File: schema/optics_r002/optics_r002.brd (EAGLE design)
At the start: 65 x 38 mm, 81 parts, among them U3 iC-HKB, X3 MikroBus_3, X4 PAN_SERVO, X5 TILT_SERVO

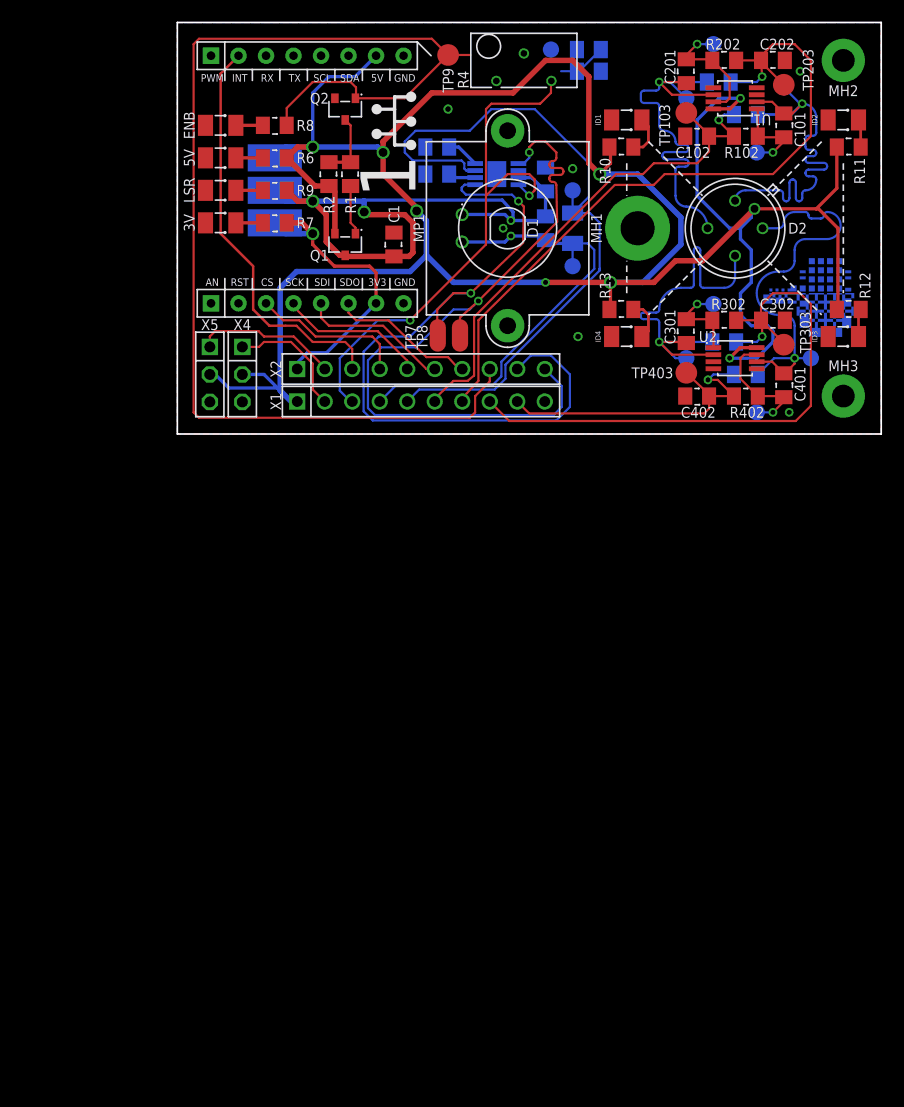
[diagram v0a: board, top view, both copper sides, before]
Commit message: updated reworks 1-4 to schematic r002
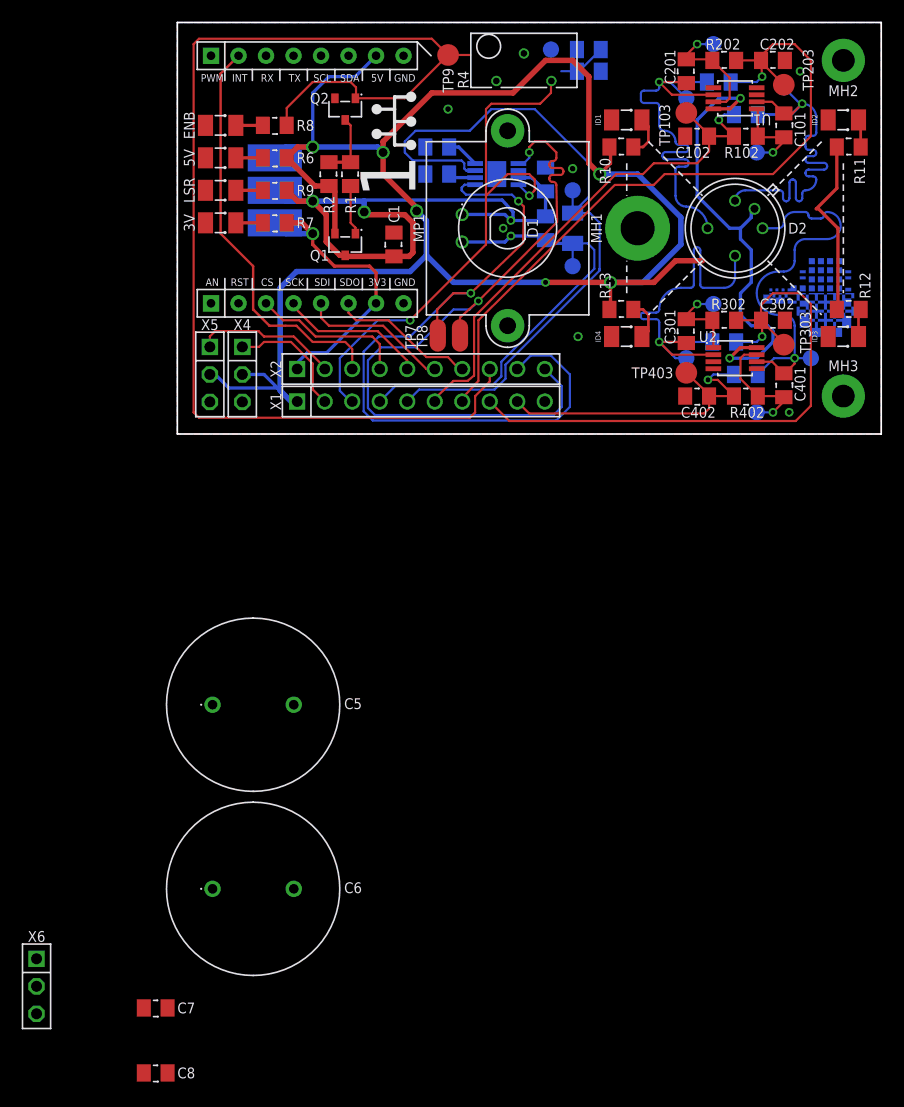
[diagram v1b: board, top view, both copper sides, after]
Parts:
- added C5, C6: 4700u, rcl:RADIAL_21_16_35
- added C7, C8: 0.1u, rcl:0805_WAVE
- added X6: REWORK, io:22-28-4030
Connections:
- new net GND_A: X6.2
- new net P12V: D2.5, X6.1
- net GND: now also C5.2, C6.2, C7.2, C8.2, X6.3
- net P5V: now also C5.1, C6.1, C7.1, C8.1; no longer D2.5
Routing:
- net P5V: track 243.3 -> 230.4 mm
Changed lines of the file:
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@@
 <attribute name="MFR" value="Cree" x="26.3" y="19" size="1.778" layer="28" rot="MR270" display="off"/>
+</element>
+<element name="C5" library="rcl" package="RADIAL_21_16_35" value="4700u" x="7" y="-25">
+<attribute name="EAGLEUP" value="RADIAL_21_16_35" x="7" y="-25" size="1.778" layer="27" display="off"/>
+<attribute name="TOL" value="20" x="7" y="-25" size="1.778" layer="27" display="off"/>
+</element>
+<element name="C6" library="rcl" package="RADIAL_21_16_35" value="4700u" x="7" y="-42">
+<attribute name="EAGLEUP" value="RADIAL_21_16_35" x="7" y="-42" size="1.778" layer="27" display="off"/>
+<attribute name="TOL" value="20" x="7" y="-42" size="1.778" layer="27" display="off"/>
+</element>
+<element name="C7" library="rcl" package="0805_WAVE" value="0.1u" x="-2" y="-53">
+<attribute name="EAGLEUP" value="C0805;;" x="-2" y="-53" size="1.778" layer="27" display="off"/>
+<attribute name="TOL" value="5" x="-2" y="-53" size="1.778" layer="27" display="off"/>
+</element>
+<element name="C8" library="rcl" package="0805_WAVE" value="0.1u" x="-2" y="-59">
+<attribute name="EAGLEUP" value="C0805;;" x="-2" y="-59" size="1.778" layer="27" display="off"/>
+<attribute name="TOL" value="5" x="-2" y="-59" size="1.778" layer="27" display="off"/>
+</element>
+<element name="X6" library="io" package="22-28-4030" value="REWORK" x="-13" y="-51">
+<attribute name="MFR" value="Molex" x="-13" y="-51" size="1.778" layer="27" display="off"/>
+<attribute name="EAGLEUP" value="HEADER_MALE_1X03;;" x="-13" y="-51" size="1.778" layer="27" display="off"/>
+<attribute name="MPN" value="22-28-4030" x="-13" y="-51" size="1.778" layer="27" display="off"/>
+<attribute name="CIRCUITS" value="3" x="-13" y="-51" size="1.778" layer="27" display="off"/>
 </element>
 </elements>
@@
 <vertex x="0" y="38"/>
 </polygon>
+<contactref element="C5" pad="2"/>
+<contactref element="C6" pad="2"/>
+<contactref element="C7" pad="2"/>
+<contactref element="C8" pad="2"/>
+<contactref element="X6" pad="3"/>
+<wire x1="57.5" y1="33.5" x2="61.5" y2="34.5" width="0" layer="19" extent="1-1"/>
+<wire x1="56.1" y1="34.5" x2="57.5" y2="33.5" width="0" layer="19" extent="1-1"/>
+<wire x1="53.5" y1="31.975" x2="56.1" y2="34.5" width="0" layer="19" extent="1-1"/>
+<wire x1="53.5" y1="31.325" x2="53.5" y2="31.975" width="0" layer="19" extent="1-1"/>
+<wire x1="49.5" y1="31.975" x2="53.5" y2="31.975" width="0" layer="19" extent="1-1"/>
+<wire x1="46.9" y1="27.5" x2="49.5" y2="31.975" width="0" layer="19" extent="1-1"/>
+<wire x1="60.1" y1="29" x2="57.5" y2="33.5" width="0" layer="19" extent="1-1"/>
+<wire x1="40.1" y1="29" x2="46.9" y2="27.5" width="0" layer="19" extent="1-1"/>
+<wire x1="39.1" y1="33.5" x2="40.1" y2="29" width="0" layer="19" extent="1-16"/>
+<wire x1="36.9" y1="35.5" x2="39.1" y2="33.5" width="0" layer="19" extent="16-16"/>
+<wire x1="36.5" y1="24.5" x2="40.1" y2="29" width="0" layer="19" extent="1-1"/>
+<wire x1="34" y1="24.6" x2="36.5" y2="24.5" width="0" layer="19" extent="16-16"/>
+<wire x1="31.5" y1="24.325" x2="34" y2="24.6" width="0" layer="19" extent="16-16"/>
+<wire x1="29.5" y1="24" x2="31.5" y2="24.325" width="0" layer="19" extent="16-16"/>
+<wire x1="30.5" y1="28" x2="31.5" y2="24.325" width="0" layer="19" extent="16-16"/>
+<wire x1="30.085" y1="19" x2="29.5" y2="24" width="0" layer="19" extent="16-16"/>
+<wire x1="25" y1="30" x2="30.5" y2="28" width="0" layer="19" extent="1-1"/>
+<wire x1="22.9" y1="26.5" x2="25" y2="30" width="0" layer="19" extent="16-16"/>
+<wire x1="22.9" y1="24" x2="22.9" y2="26.5" width="0" layer="19" extent="16-16"/>
+<wire x1="20" y1="18.6" x2="22.9" y2="24" width="0" layer="19" extent="1-16"/>
+<wire x1="20.89" y1="34.93" x2="25" y2="30" width="0" layer="19" extent="1-1"/>
+<wire x1="20.89" y1="12.07" x2="20" y2="18.6" width="0" layer="19" extent="1-1"/>
+<wire x1="14.55" y1="31" x2="20.89" y2="34.93" width="0" layer="19" extent="1-1"/>
+<wire x1="42.5" y1="19" x2="36.5" y2="24.5" width="0" layer="19" extent="1-1"/>
+<wire x1="30.5" y1="10" x2="30.085" y2="19" width="0" layer="19" extent="1-1"/>
+<wire x1="37" y1="9" x2="30.5" y2="10" width="0" layer="19" extent="1-1"/>
+<wire x1="40.1" y1="9" x2="37" y2="9" width="0" layer="19" extent="1-1"/>
+<wire x1="33.93" y1="3" x2="37" y2="9" width="0" layer="19" extent="1-1"/>
+<wire x1="46.9" y1="3.5" x2="40.1" y2="9" width="0" layer="19" extent="1-1"/>
+<wire x1="49.5" y1="6.025" x2="46.9" y2="3.5" width="0" layer="19" extent="1-1"/>
+<wire x1="49.5" y1="6.675" x2="49.5" y2="6.025" width="0" layer="19" extent="1-1"/>
+<wire x1="53.5" y1="6.025" x2="49.5" y2="6.025" width="0" layer="19" extent="1-1"/>
+<wire x1="56.5" y1="2" x2="53.5" y2="6.025" width="0" layer="19" extent="1-1"/>
+<wire x1="56.1" y1="10.5" x2="53.5" y2="6.025" width="0" layer="19" extent="1-1"/>
+<wire x1="60.1" y1="9" x2="56.1" y2="10.5" width="0" layer="19" extent="1-1"/>
+<wire x1="61.5" y1="3.5" x2="56.5" y2="2" width="0" layer="19" extent="1-1"/>
+<wire x1="2.6" y1="28.5" x2="14.55" y2="31" width="0" layer="19" extent="1-1"/>
+<wire x1="2.6" y1="25.5" x2="2.6" y2="28.5" width="0" layer="19" extent="1-1"/>
+<wire x1="2.6" y1="22.5" x2="2.6" y2="25.5" width="0" layer="19" extent="1-1"/>
+<wire x1="2.6" y1="19.5" x2="2.6" y2="22.5" width="0" layer="19" extent="1-1"/>
+<wire x1="3" y1="2.96" x2="2.6" y2="19.5" width="0" layer="19" extent="1-1"/>
+<wire x1="6" y1="2.96" x2="3" y2="2.96" width="0" layer="19" extent="1-1"/>
+<wire x1="10.75" y1="-25" x2="6" y2="2.96" width="0" layer="19" extent="1-1"/>
+<wire x1="10.75" y1="-42" x2="10.75" y2="-25" width="0" layer="19" extent="1-1"/>
+<wire x1="-3.1" y1="-53" x2="10.75" y2="-42" width="0" layer="19" extent="1-1"/>
+<wire x1="-3.1" y1="-59" x2="-3.1" y2="-53" width="0" layer="19" extent="1-1"/>
+<wire x1="-13" y1="-53.54" x2="-3.1" y2="-53" width="0" layer="19" extent="1-1"/>
 </signal>
 <signal name="LSR_ENB_NMOS_DRAIN">
@@
 <contactref element="TP1" pad="1"/>
 <contactref element="U1" pad="8"/>
-<contactref element="D2" pad="5"/>
 <contactref element="U2" pad="8"/>
 <contactref element="X5" pad="2"/>
@@
 <wire x1="52" y1="19" x2="53" y2="20" width="0.3048" layer="16"/>
 <wire x1="53" y1="20" x2="53" y2="20.5" width="0.3048" layer="16"/>
-<wire x1="53" y1="20.5" x2="53.29605" y2="20.79605" width="0.3048" layer="16"/>
 <wire x1="53.5" y1="7" x2="51" y2="7" width="0.3048" layer="16"/>
 <via x="51" y="7" extent="1-16" drill="0.4572"/>
@@
 <wire x1="44" y1="14" x2="46" y2="16" width="0.508" layer="1"/>
 <wire x1="46" y1="16" x2="48.5" y2="16" width="0.508" layer="1"/>
-<wire x1="48.5" y1="16" x2="53.29605" y2="20.79605" width="0.508" layer="1"/>
 <wire x1="19" y1="26" x2="19" y2="27" width="0.508" layer="1"/>
 <wire x1="19" y1="27" x2="23.5" y2="31.5" width="0.508" layer="1"/>
@@
 <via x="22.1" y="20.6" extent="1-16" drill="0.8128"/>
 <wire x1="22.1" y1="20.6" x2="23" y2="19.7" width="0.508" layer="16"/>
-<wire x1="53.29605" y1="20.79605" x2="59" y2="20.79605" width="0.3048" layer="1"/>
 <wire x1="59" y1="20.79605" x2="59.20395" y2="20.79605" width="0.3048" layer="1"/>
 <wire x1="59.20395" y1="20.79605" x2="61" y2="19" width="0.3048" layer="1"/>
@@
 <wire x1="55" y1="9.5" x2="55" y2="8.5" width="0.3048" layer="16"/>
 <wire x1="55" y1="8.5" x2="53.5" y2="7" width="0.3048" layer="16"/>
+<contactref element="C5" pad="1"/>
+<contactref element="C6" pad="1"/>
+<contactref element="C8" pad="1"/>
+<contactref element="C7" pad="1"/>
+<wire x1="53" y1="20.5" x2="59" y2="20.79605" width="0" layer="19" extent="1-16"/>
+<wire x1="46.5" y1="20" x2="48" y2="22" width="0" layer="19" extent="16-16"/>
+<wire x1="3.25" y1="-25" x2="10.5" y2="3" width="0" layer="19" extent="16-16"/>
+<wire x1="3.25" y1="-42" x2="3.25" y2="-25" width="0" layer="19" extent="1-1"/>
+<wire x1="-0.9" y1="-53" x2="3.25" y2="-42" width="0" layer="19" extent="1-1"/>
+<wire x1="-0.9" y1="-59" x2="-0.9" y2="-53" width="0" layer="19" extent="1-1"/>
 </signal>
 <signal name="P3_3V" class="1">
@@
 <wire x1="43" y1="9" x2="42.9" y2="9" width="0.254" layer="1"/>
 </signal>
+<signal name="P12V">
+<contactref element="D2" pad="5"/>
+<contactref element="X6" pad="1"/>
+<wire x1="-13" y1="-48.46" x2="53.29605" y2="20.79605" width="0" layer="19" extent="1-1"/>
+</signal>
+<signal name="GND_A">
+<contactref element="X6" pad="2"/>
+</signal>
 </signals>
